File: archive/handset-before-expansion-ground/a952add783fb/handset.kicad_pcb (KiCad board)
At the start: 4 copper layers, 66 x 142 mm, 263 parts, among them J1 2053380002, J10 LF_COIL_TUNING_REQUIRED, J16 EXPANSION_J16, J2 PACK_NTC_10K_B3435, J20 LORA_915_ANT, J21 CC1101_915_ANT, J22 GNSS_PASSIVE_ANT, J23 DM3D-SF, J24 TSAL6400_CASE_LED, J25 TSOP38438_CASE_RX, J26 FH12A-50S-0.5SH(55), J3 MEDIA_SPEAKER_DIFFERENTIAL, J4 CALL_AUDIO_FROM_MODEM_ADAPTER, J5 CALL_EARPIECE, J6 CALL_MIC, J7 PIM447_HARNESS_VERIFY, J8 MODEM_ADAPTER_3V3_LOGIC, J9 MODEM_POWER_ADAPTER_REQUIRED, Q1 AO3400A, Q3 AO3400A, Q4 AO3400A, Q5 AO3400A, Q6 AO3401A, Q7 AO3400A, Q8 AO3400A, SW1 1, SW10 10, SW11 11, SW12 12, SW13 13, SW14 14, SW15 15, SW16 16, SW17 MCU_BOOT, SW18 MCU_EN, SW19 POWER, SW2 2, SW3 3, SW4 4, SW5 5, SW6 6, SW7 7, SW8 8, SW9 9, U1 ESP32-S3-WROOM-1-N16R8, U10 TPS61023DRLR, U11 TPS62840DLCR, U12 MAX-M10S-00B-01, U13 ST25R3916B-AQET, U14 TPS2553DBVR, U15 TPD4E05U06DQAR, U16 TPD4E05U06DQAR, U17 TPD4E05U06DQAR, U18 SN74AHCT125PWR, U19 SN74LVC1G17DBVR, U2 TCA8418RTWR, U20 TPS63070RNMR, U21 TPS25200DRVR, U22 TUSB320LAIRWBR, U23 TLV70433DBVR, U24 TCA9536DGKR, U25 STM32G031G8U6, U26 TPS7A0230PDBVR, U27 TCA9800DGKR, U28 TPS7A2030PDBVR, U29 SN74LVC244APWR, U3 BQ25186DLHR, U30 SN74LVC2G125DCUR, U31 TCA9406DCUR, U32 CAT4004AHU2-GT3, U33 TCA9537DGSR, U34 SN74CB3Q3245PWR, U35 SN74HCS10PWR, U4 SX1262IMLTRT, U5 CC1101RGPR, U6 MAX98357AETE+, U7 TPS63802DLAR, U8 MAX17048G+T, U9 HTRC11001T, Y1 ABM8-27.120MHZ-B2-T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

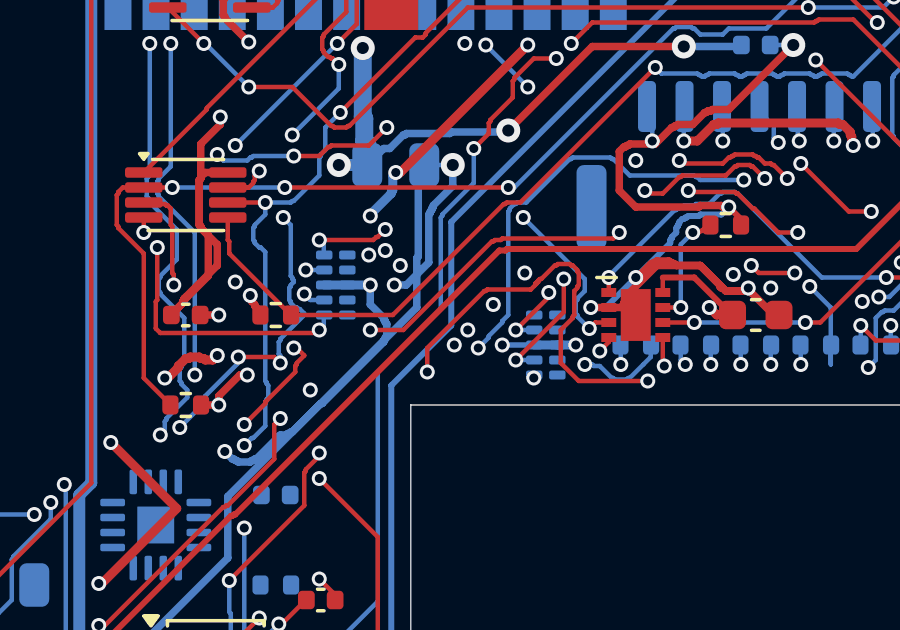
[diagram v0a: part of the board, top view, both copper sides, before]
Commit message: fix: shorten expansion ESD ground returns
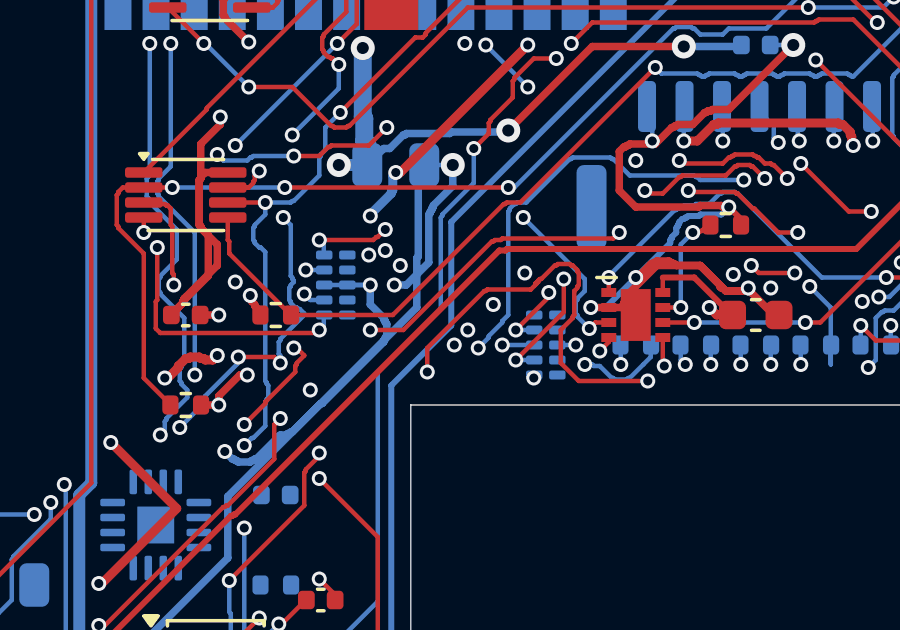
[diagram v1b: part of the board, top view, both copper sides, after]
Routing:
- net GND: track 334.2 -> 366.5 mm
- removed copper zone on In2.Cu, net GND
